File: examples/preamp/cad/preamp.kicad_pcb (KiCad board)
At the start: 2 copper layers, 55 parts, among them CON1 AVR-ISP-10, J1 Conn_01x04, J10 Conn_01x03, J11 Conn_01x03, J12 CONN_01X02, J13 CONN_01X03, J14 Conn_01x04, J15 Conn_01x04, J16 Conn_01x04, J2 Conn_01x04, J3 Conn_01x03, J4 Conn_01x03, J5 Conn_01x03, J6 Conn_01x03, J7 Conn_01x04, J8 CONN_01X03, J9 Conn_01x03, Q1 ., Q2 ., U1 ATMEGA8A-PU, U2 DS1307+, U3 LM7809CT, U4 TDA7313, Y1 Crystal

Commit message: Update preamp scheme
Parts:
- J1, J2, J7: footprint Connector_PinHeader_2.54mm:PinHeader_1x04_P2.54mm_Vertical -> Connector_JST:JST_EH_B4B-EH-A_1x04_P2.50mm_Vertical
- J10, J3, J4, J5, J6: value Conn_01x03 -> Conn_01x04; footprint Connector_PinHeader_2.54mm:PinHeader_1x03_P2.54mm_Vertical -> Connector_JST:JST_EH_B4B-EH-A_1x04_P2.50mm_Vertical
- J11: value Conn_01x03 -> CONN_01X03; footprint Connector_PinHeader_2.54mm:PinHeader_1x03_P2.54mm_Vertical -> Connector_JST:JST_EH_B3B-EH-A_1x03_P2.50mm_Vertical
- J12: value CONN_01X02 -> Conn_01x03; footprint Connector_PinHeader_2.54mm:PinHeader_1x02_P2.54mm_Vertical -> TerminalBlock_Phoenix:TerminalBlock_Phoenix_MKDS-3-3-5.08_1x03_P5.08mm_Horizontal
- J13: value CONN_01X03 -> Conn_01x03; footprint Connector_PinHeader_2.54mm:PinHeader_1x03_P2.54mm_Vertical -> TerminalBlock_Phoenix:TerminalBlock_Phoenix_MKDS-3-3-5.08_1x03_P5.08mm_Horizontal
- J14: value Conn_01x04 -> Conn_01x03; footprint Connector_PinHeader_2.54mm:PinHeader_1x04_P2.54mm_Vertical -> TerminalBlock_Phoenix:TerminalBlock_Phoenix_MKDS-3-3-5.08_1x03_P5.08mm_Horizontal
- J15: value Conn_01x04 -> CONN_01X02; footprint Connector_PinHeader_2.54mm:PinHeader_1x04_P2.54mm_Vertical -> Connector_JST:JST_EH_B3B-EH-A_1x03_P2.50mm_Vertical
- J16: value Conn_01x04 -> CONN_01X03; footprint Connector_PinHeader_2.54mm:PinHeader_1x04_P2.54mm_Vertical -> TerminalBlock_Phoenix:TerminalBlock_Phoenix_MKDS-3-3-5.08_1x03_P5.08mm_Horizontal
- J8: value CONN_01X03 -> Conn_01x04; footprint Connector_PinHeader_2.54mm:PinHeader_1x03_P2.54mm_Vertical -> Connector_JST:JST_EH_B4B-EH-A_1x04_P2.50mm_Vertical
- J9: footprint Connector_PinHeader_2.54mm:PinHeader_1x03_P2.54mm_Vertical -> Connector_JST:JST_EH_B3B-EH-A_1x03_P2.50mm_Vertical
- moved U3 161.3 mm to (163.8, 38.1)
- moved C12 161.3 mm to (165.1, 21.6)
- moved C13 161.3 mm to (153.7, 40.6)
- moved C15 161.3 mm to (151.2, 30.5)
- moved C8 161.3 mm to (162.7, 30.5)
- moved J12 158.3 mm to (190.5, 100.3), turned to 180 degrees
- moved C23 152.2 mm to (200.7, 49.5), turned to 270 degrees
- moved C16 148.4 mm to (205.7, 49.5), turned to 270 degrees
- moved C14 136.9 mm to (184.2, 49.5), turned to 0 degrees
- moved C7 135.4 mm to (201.9, 85.1), turned to 270 degrees
- moved C20 131.7 mm to (201.9, 64.8)
- moved C19 122.1 mm to (191.8, 55.9), turned to 180 degrees
- moved C11 119.8 mm to (185.4, 59.7), turned to 270 degrees
- moved C4 119.5 mm to (195.6, 85.1), turned to 270 degrees
- moved J13 115.3 mm to (208.3, 100.3), turned to 180 degrees
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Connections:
- net /PowerLED renamed Net-(J3-Pad1)
- CON1 pad 2: Net-(CON1-Pad2) -> VCC
- CON1 pad 7: /SCK -> /Input1BTN_SCK
- J10 pad 1: GNDA -> GND
- J10 pad 2: Net-(C7-Pad2) -> VCC
- J10 pad 3: Net-(C4-Pad2) -> /SDA
- J11 pad 1: GNDA -> VCC
- J11 pad 2: Net-(C9-Pad2) -> /IRint
- J11 pad 3: Net-(C5-Pad2) -> GND
- J12 pad 2: Net-(C12-Pad1) -> Net-(C6-Pad2)
- J13 pad 1: /LEFT -> GNDA
- J13 pad 2: /RIGHT -> Net-(C7-Pad2)
- J13 pad 3: GNDA -> Net-(C4-Pad2)
- J14 pad 1: GND -> GNDA
- J14 pad 2: /Input1Btn -> Net-(C9-Pad2)
- J14 pad 3: /Input1Led -> Net-(C5-Pad2)
- J15 pad 1: GND -> GNDA
- J15 pad 2: /Input2Btn -> Net-(C12-Pad1)
- J15 pad 3: /Input2Led -> (no net)
- J16 pad 1: GND -> /LEFT
- J16 pad 2: /Input3Btn -> /RIGHT
- J16 pad 3: /Input3Led -> GNDA
- J3 pad 2: /BTN3_MOSI -> /PowerLEDGND
- J3 pad 3: VCC -> /BTN3_MOSI
- J4 pad 2: /BTN1 -> /PowerLEDGND
- J4 pad 3: VCC -> /BTN1
- J5 pad 2: /BTN0 -> /PowerLEDGND
- J5 pad 3: VCC -> /BTN0
- J6 pad 1: Net-(J6-Pad1) -> GND
- J6 pad 2: VCC -> /Input1BTN_SCK
- J6 pad 3: GND -> /Input1Led
- J7 pad 2: VCC -> /Input2Btn
- J7 pad 3: /SDA -> /Input2Led
- J7 pad 4: /SCL -> VCC
- J8 pad 1: VCC -> GND
- J8 pad 2: /IRint -> /Input3Btn
- J8 pad 3: GND -> /Input3Led
- J9 pad 1: GNDA -> Net-(J9-Pad1)
- J9 pad 2: Net-(C6-Pad2) -> VCC
- J9 pad 3: Net-(C3-Pad2) -> GND
- Q1 pad 2: Net-(J6-Pad1) -> Net-(J9-Pad1)
- U1 pad 10: Net-(U1-Pad10) -> /Input3Btn
- U1 pad 19: /SCK -> /Input1BTN_SCK
- U1 pad 2: Net-(U1-Pad2) -> /StandBy
- U1 pad 9: Net-(U1-Pad9) -> /Input2Btn

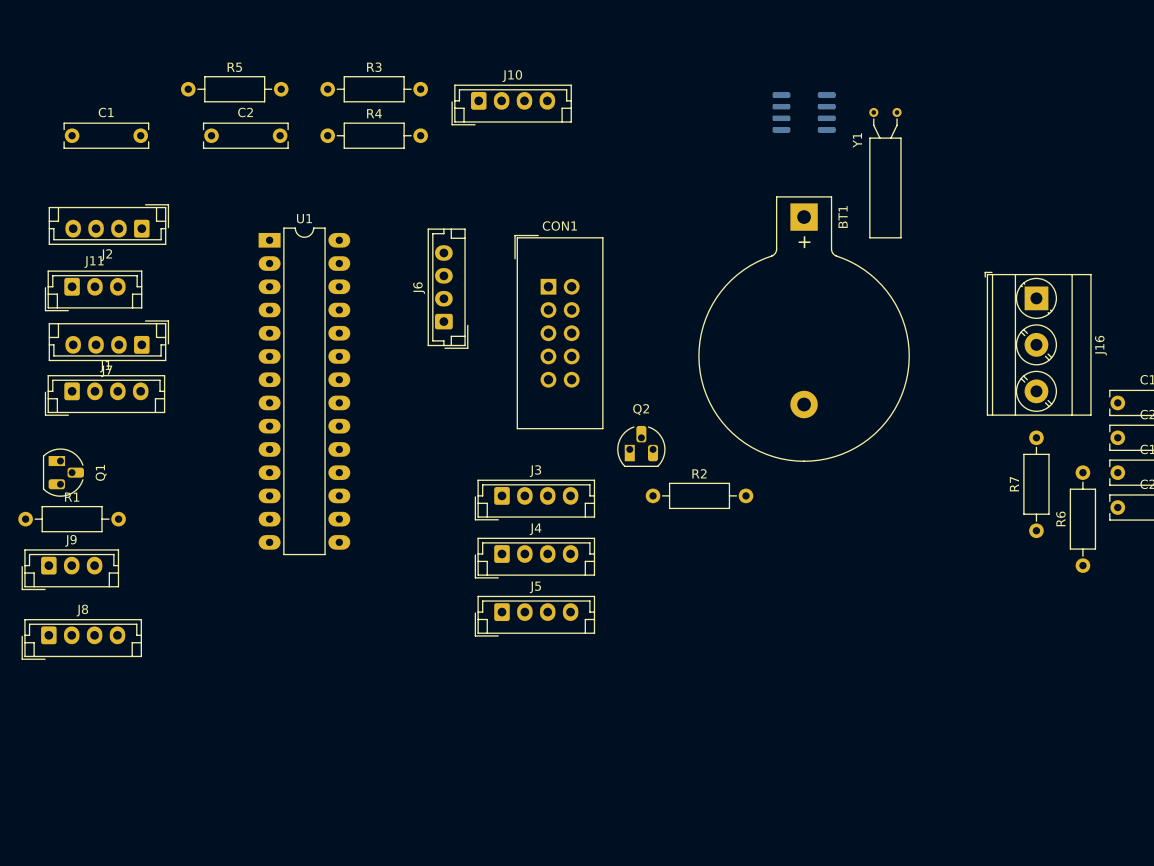
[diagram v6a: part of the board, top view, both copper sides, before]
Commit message: Update preamp scheme: add led resistors
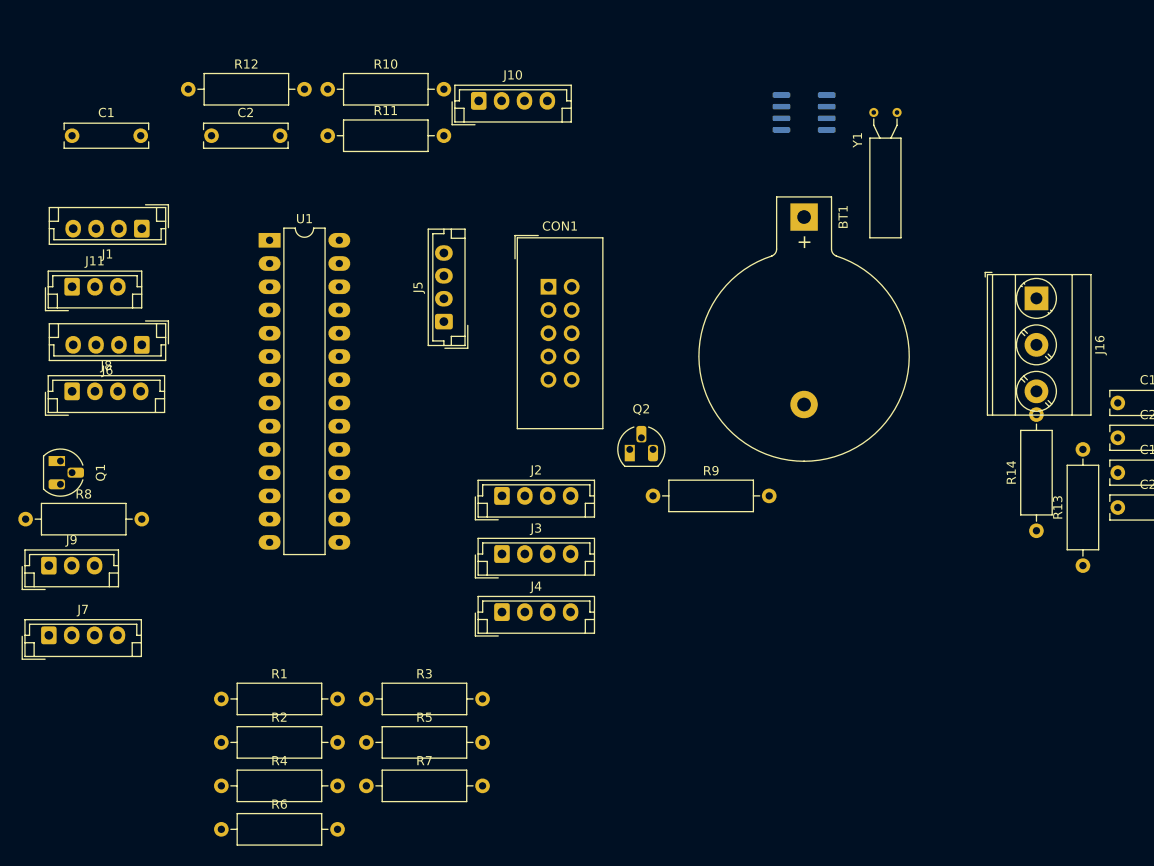
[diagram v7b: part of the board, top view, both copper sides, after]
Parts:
- added R10: 10k, Resistor_THT:R_Axial_DIN0309_L9.0mm_D3.2mm_P12.70mm_Horizontal, F.Cu at (53.3, 25.4)
- added R11: 10k, Resistor_THT:R_Axial_DIN0309_L9.0mm_D3.2mm_P12.70mm_Horizontal, F.Cu at (53.3, 30.5)
- added R12: 10k, Resistor_THT:R_Axial_DIN0309_L9.0mm_D3.2mm_P12.70mm_Horizontal, F.Cu at (38.1, 25.4)
- added R13: 5.6k, Resistor_THT:R_Axial_DIN0309_L9.0mm_D3.2mm_P12.70mm_Horizontal, F.Cu at (135.9, 77.5)
- added R14: 5.6k, Resistor_THT:R_Axial_DIN0309_L9.0mm_D3.2mm_P12.70mm_Horizontal, F.Cu at (130.8, 73.7)
- added R8: 10k, Resistor_THT:R_Axial_DIN0309_L9.0mm_D3.2mm_P12.70mm_Horizontal, F.Cu at (20.3, 72.4)
- added R9: 10k, Resistor_THT:R_Axial_DIN0309_L9.0mm_D3.2mm_P12.70mm_Horizontal, F.Cu at (88.9, 69.8)
- R1, R2, R3, R4, R5: value 10k -> 1k; footprint Resistor_THT:R_Axial_DIN0207_L6.3mm_D2.5mm_P10.16mm_Horizontal -> Resistor_THT:R_Axial_DIN0309_L9.0mm_D3.2mm_P12.70mm_Horizontal
- R6, R7: value 5.6k -> 1k; footprint Resistor_THT:R_Axial_DIN0207_L6.3mm_D2.5mm_P10.16mm_Horizontal -> Resistor_THT:R_Axial_DIN0309_L9.0mm_D3.2mm_P12.70mm_Horizontal
- moved R6 98.5 mm to (41.7, 106.3), turned to 0 degrees
- moved R7 78.4 mm to (57.6, 101.5), turned to 0 degrees
- moved R5 74.0 mm to (57.6, 96.8)
- moved R4 72.0 mm to (41.7, 101.5)
- moved R3 66.8 mm to (57.6, 92.0)
- moved R2 54.3 mm to (41.7, 96.8)
- moved R1 29.1 mm to (41.7, 92.0)
- renumbered J2 to J1, J3 to J2, J4 to J3, J5 to J4, J6 to J5, J7 to J6, J8 to J7, J1 to J8
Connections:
- J1 pad 3: /StandBy -> Net-(J1-Pad3)
- J2 pad 2: /PowerLEDGND -> Net-(J2-Pad2)
- J3 pad 2: /PowerLEDGND -> Net-(J3-Pad2)
- J4 pad 2: /PowerLEDGND -> Net-(J4-Pad2)
- J5 pad 3: /Input1Led -> Net-(J5-Pad3)
- J6 pad 3: /Input2Led -> Net-(J6-Pad3)
- J7 pad 3: /Input3Led -> Net-(J7-Pad3)
- Q2 pad 2: Net-(Q2-Pad2) -> /PowerLEDGND
- R1 pad 1: Net-(Q1-Pad1) -> /StandBy
- R1 pad 2: /Power -> Net-(J1-Pad3)
- R2 pad 1: Net-(Q2-Pad1) -> /PowerLEDGND
- R2 pad 2: /Power -> Net-(J2-Pad2)
- R3 pad 1: VCC -> /PowerLEDGND
- R3 pad 2: /SCL -> Net-(J3-Pad2)
- R4 pad 1: VCC -> /PowerLEDGND
- R4 pad 2: /SDA -> Net-(J4-Pad2)
- R5 pad 1: VCC -> /Input1Led
- R5 pad 2: /Reset -> Net-(J5-Pad3)
- R6 pad 1: GNDA -> /Input2Led
- R6 pad 2: Net-(C17-Pad1) -> Net-(J6-Pad3)
- R7 pad 1: GNDA -> /Input3Led
- R7 pad 2: Net-(C18-Pad1) -> Net-(J7-Pad3)

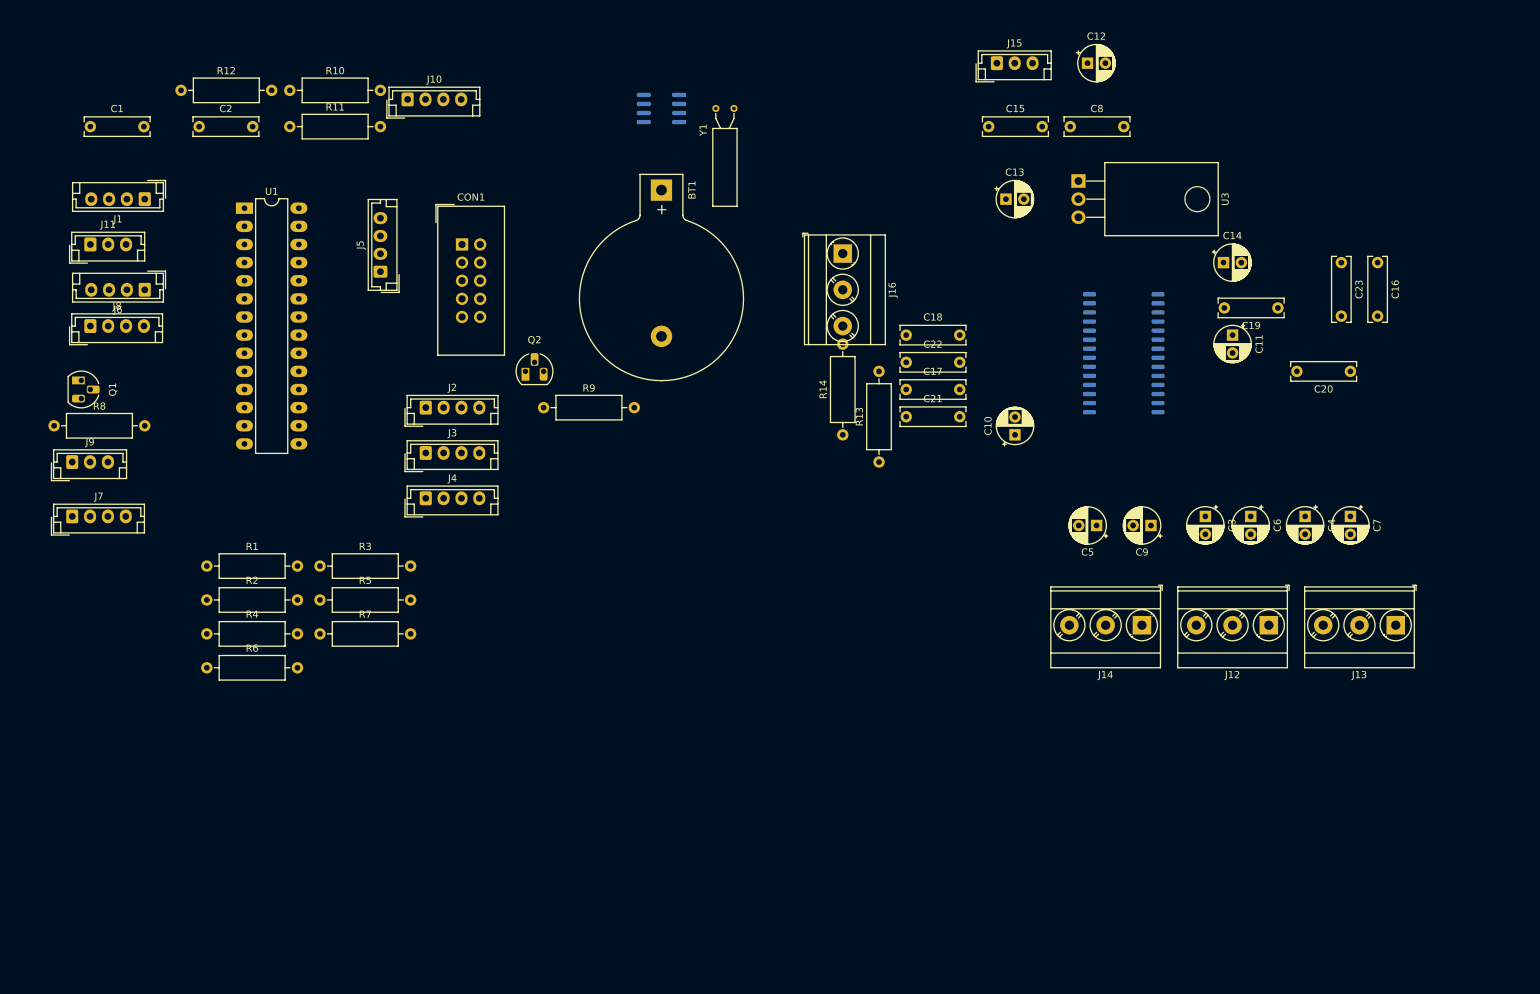
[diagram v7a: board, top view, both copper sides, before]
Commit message: Update preamp scheme: add +5V power
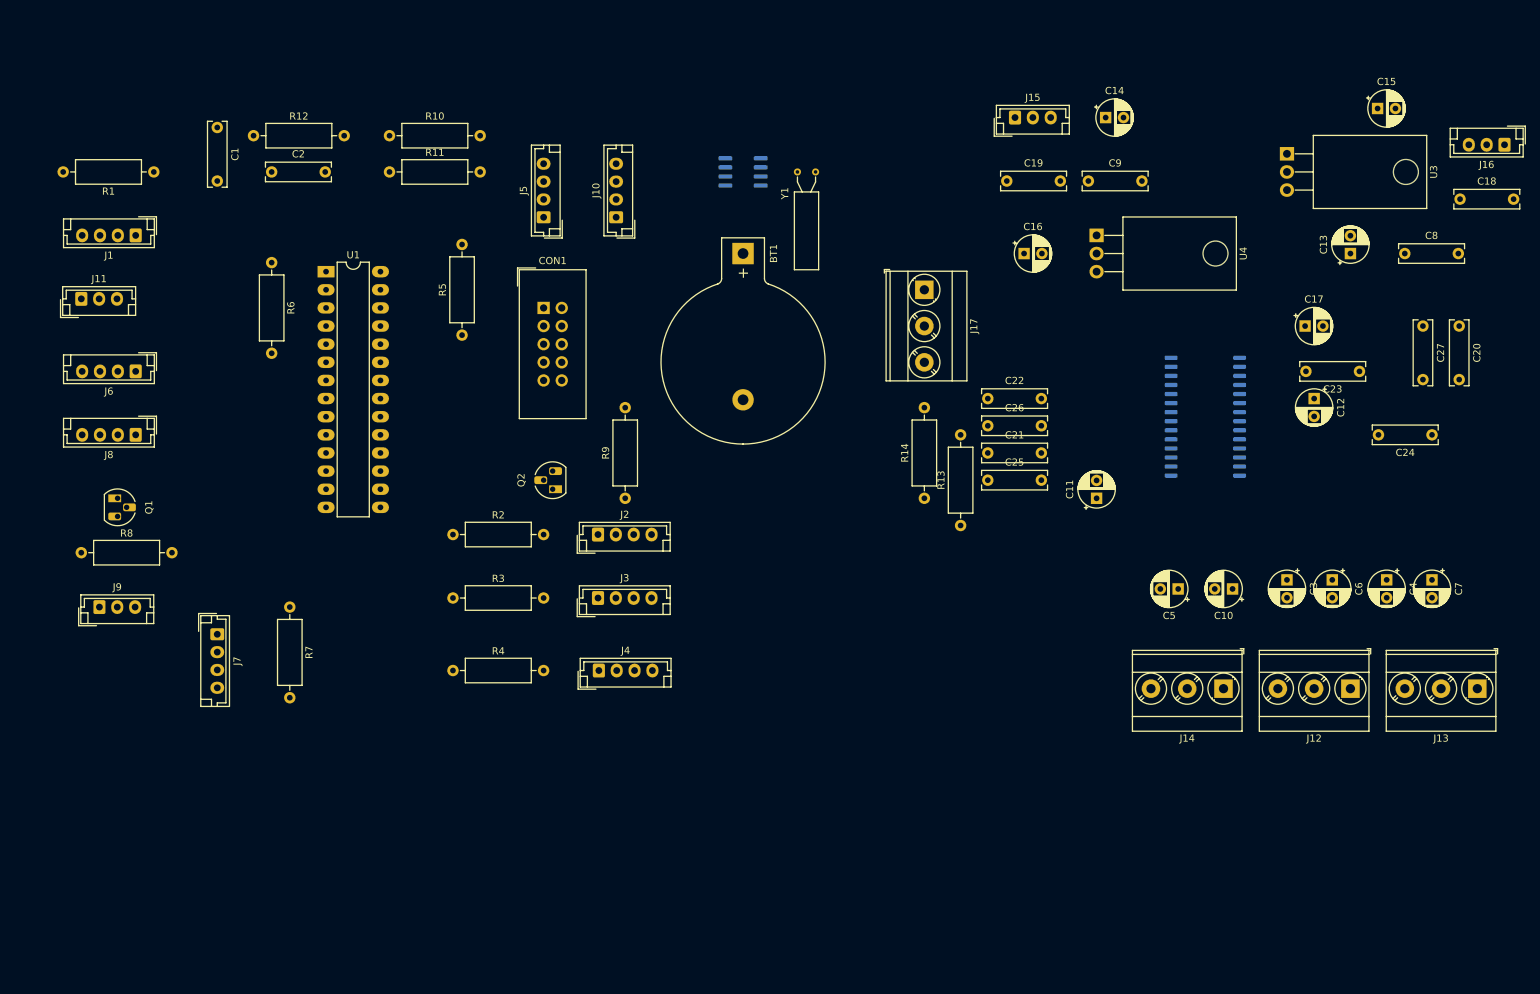
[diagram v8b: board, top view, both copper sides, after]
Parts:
- added C13: 100uF, Capacitor_THT:CP_Radial_D5.0mm_P2.50mm, F.Cu at (201.9, 48.3)
- added C15: 100uF, Capacitor_THT:CP_Radial_D5.0mm_P2.50mm, F.Cu at (205.7, 27.9)
- added C18: 100nF, Capacitor_THT:C_Rect_L9.0mm_W2.5mm_P7.50mm_MKT, F.Cu at (217.3, 40.6)
- added C8: 0.33uF, Capacitor_THT:C_Rect_L9.0mm_W2.5mm_P7.50mm_MKT, F.Cu at (209.6, 48.3)
- added J16: CONN_01X03, Connector_JST:JST_EH_B3B-EH-A_1x03_P2.50mm_Vertical, F.Cu at (223.5, 33.0)
- added U3: LM7805, Package_TO_SOT_THT:TO-220-3_Horizontal_TabDown, F.Cu at (193.0, 34.3)
- J15: value CONN_01X02 -> CONN_01X03
- moved R6 57.5 mm to (50.8, 49.5), turned to 270 degrees
- moved R1 55.7 mm to (34.3, 36.8), turned to 180 degrees
- moved R5 42.1 mm to (77.5, 59.7), turned to 90 degrees
- moved R2 35.7 mm to (76.2, 87.6)
- moved R4 34.9 mm to (76.2, 106.7)
- moved J4 34.2 mm to (96.6, 106.7)
- moved J10 33.6 mm to (99.1, 43.2), turned to 90 degrees
- moved J3 31.5 mm to (96.5, 96.5)
- moved J2 30.0 mm to (96.5, 87.6)
- moved J7 26.2 mm to (43.2, 101.6), turned to 270 degrees
- moved J5 24.1 mm to (88.9, 43.2)
- moved J9 20.7 mm to (26.7, 97.8)
- moved R3 19.2 mm to (76.2, 96.5)
- moved R8 18.2 mm to (24.1, 90.2)
- moved C1 17.8 mm to (43.2, 30.6), turned to 270 degrees
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- renumbered C9 to C10, C10 to C11, C11 to C12, C12 to C14, C13 to C16, C14 to C17, C15 to C19, C16 to C20, C17 to C21, C18 to C22, C19 to C23, C20 to C24, C21 to C25, C22 to C26, C23 to C27, C8 to C9, J16 to J17, U3 to U4, U4 to U5
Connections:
- J15 pad 3: (no net) -> Net-(J15-Pad3)
